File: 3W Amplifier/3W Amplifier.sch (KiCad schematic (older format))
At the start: 20 parts, among them SW1 SW_DIP_x02, U1 PAM8008

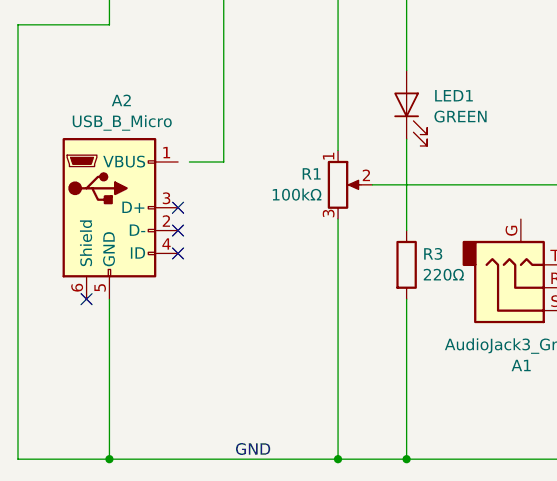
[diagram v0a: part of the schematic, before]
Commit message: Add the shield pins back onto the USB connector and connect to GND
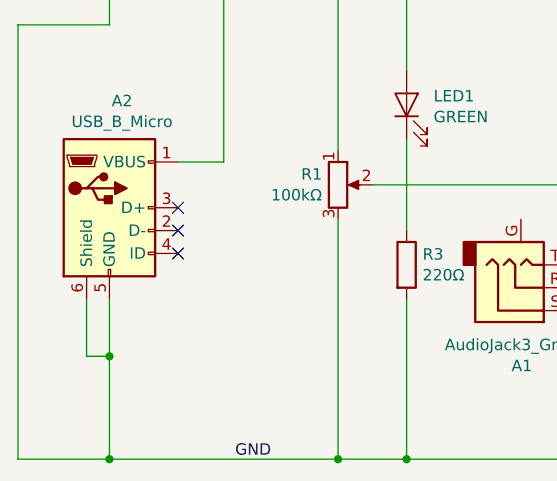
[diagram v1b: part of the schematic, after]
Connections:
- net GND: now also A2.6 (Shield)
- net at A2.1 (VBUS): now also SW1.1
- no-connect marks 6 -> 5
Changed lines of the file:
@@
 	0    -1   -1   0
 $EndComp
-NoConn ~ 2600 4300
 NoConn ~ 3000 3900
 NoConn ~ 3000 4000
@@
 	2700 5000 3700 5000
 Wire Wire Line
-	2700 4300 2700 5000
+	2700 4300 2700 4550
 Connection ~ 3700 5000
 $Comp
@@
 	2700 2250 2700 2500
 Wire Wire Line
-	3050 3700 3200 3700
-Wire Wire Line
 	3200 3700 3200 2850
 Wire Wire Line
@@
 	3700 2250 3300 2250
 Connection ~ 3700 2400
+Wire Wire Line
+	3000 3700 3200 3700
+Wire Wire Line
+	2600 4300 2600 4550
+Wire Wire Line
+	2600 4550 2700 4550
+Connection ~ 2700 4550
+Wire Wire Line
+	2700 4550 2700 5000
 $EndSCHEMATC
